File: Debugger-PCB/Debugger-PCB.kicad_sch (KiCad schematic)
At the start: 0 parts

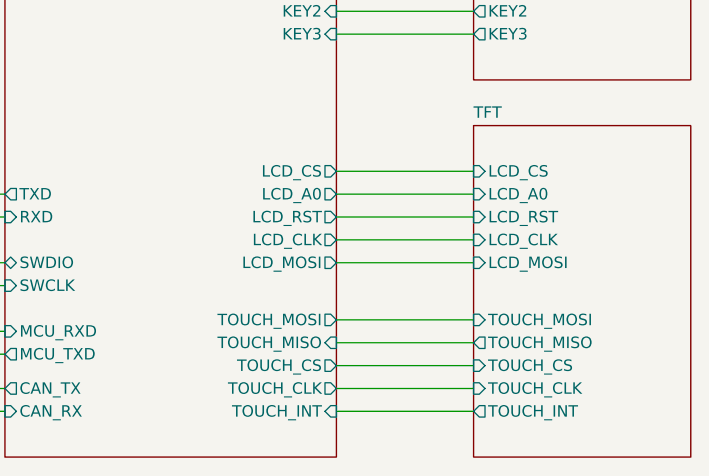
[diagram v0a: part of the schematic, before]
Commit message: fix some details of PCB
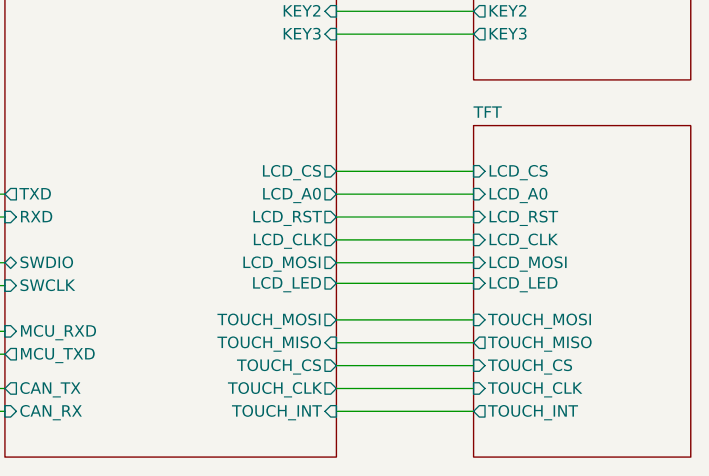
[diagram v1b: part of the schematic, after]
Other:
- sheet MCU ports: added LCD_LED; removed none
- sheet TFT ports: added LCD_LED; removed none
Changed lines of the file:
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@@
+    (stroke (width 0) (type default) (color 0 0 0 0))
+  )
+  (wire (pts (xy 222.25 159.766) (xy 237.49 159.766))
     (stroke (width 0) (type default) (color 0 0 0 0))
   )
@@
       (effects (font (size 1.27 1.27)) (justify left))
     )
+    (pin "LCD_LED" input (at 237.49 159.766 180)
+      (effects (font (size 1.27 1.27)) (justify left))
+    )
   )
   (sheet (at 185.42 114.3) (size 36.83 64.77) (fields_autoplaced)
@@
     )
     (pin "KEY3" input (at 222.25 132.08 0)
+      (effects (font (size 1.27 1.27)) (justify right))
+    )
+    (pin "LCD_LED" output (at 222.25 159.766 0)
       (effects (font (size 1.27 1.27)) (justify right))
     )
@@
       (reference "#PWR057") (unit 1) (value "VCC") (footprint "")
     )
-    (path "/98507381-f2ba-4111-8a0c-685d3bb1dc73/edf7fd00-56a4-4615-95df-5a269d3d723f"
-      (reference "#PWR058") (unit 1) (value "VCC") (footprint "")
-    )
     (path "/98507381-f2ba-4111-8a0c-685d3bb1dc73/6f52f786-b4c0-44b2-8071-17e39d084c29"
       (reference "#PWR059") (unit 1) (value "GND") (footprint "")
@@
       (reference "#PWR062") (unit 1) (value "GND") (footprint "")
     )
-    (path "/98507381-f2ba-4111-8a0c-685d3bb1dc73/292a4533-a85c-478c-bb48-f8e44071f858"
-      (reference "#PWR063") (unit 1) (value "GND") (footprint "")
-    )
-    (path "/98507381-f2ba-4111-8a0c-685d3bb1dc73/25948667-45ee-4c9f-9351-e19cee2c4d2a"
-      (reference "#PWR064") (unit 1) (value "GND") (footprint "")
-    )
     (path "/f62c1f79-9897-417c-80b5-375c0b215cca/4a0eda2d-a0f5-4497-b46a-c4cec8ad4931"
       (reference "#PWR0101") (unit 1) (value "VCC") (footprint "")
@@
       (reference "#PWR0103") (unit 1) (value "VCC") (footprint "")
     )
+    (path "/42df1dfa-ab2e-460c-8753-1de9db40f85a/baab9947-9bf5-42ec-8dc5-e6ae9b5f2e9b"
+      (reference "#PWR0104") (unit 1) (value "GND") (footprint "")
+    )
+    (path "/42df1dfa-ab2e-460c-8753-1de9db40f85a/f939aabb-c7c0-47c1-b5fa-85c2748b9d86"
+      (reference "#PWR0105") (unit 1) (value "GND") (footprint "")
+    )
+    (path "/b0467b07-32de-468c-a83e-6fe96781bcfe/2d9aa523-584c-4e58-ae94-1b029770dc75"
+      (reference "#PWR0106") (unit 1) (value "GND") (footprint "")
+    )
     (path "/42df1dfa-ab2e-460c-8753-1de9db40f85a/540b8823-2d1b-4a52-81d3-ade6ac974afd"
       (reference "C1") (unit 1) (value "10u") (footprint "Capacitor_SMD:C_0603_1608Metric")
@@
       (reference "C27") (unit 1) (value "100n") (footprint "Capacitor_SMD:C_0603_1608Metric")
     )
-    (path "/98507381-f2ba-4111-8a0c-685d3bb1dc73/6a646482-4975-41ee-9572-2521e9033ad1"
-      (reference "C28") (unit 1) (value "100n") (footprint "Capacitor_SMD:C_0603_1608Metric")
-    )
     (path "/42df1dfa-ab2e-460c-8753-1de9db40f85a/5e8b8d06-e040-4890-a404-eecea5d84e0f"
       (reference "D1") (unit 1) (value "LED") (footprint "LED_SMD:LED_0603_1608Metric")
@@
       (reference "LCD1") (unit 1) (value "1.8inch-TFT-LCD") (footprint "debugger:TFT-LCD1.8inch")
     )
+    (path "/b0467b07-32de-468c-a83e-6fe96781bcfe/99520a95-636f-4c5f-8c4f-c2d2aa10850a"
+      (reference "Q1") (unit 1) (value "S8050") (footprint "Package_TO_SOT_SMD:SOT-23")
+    )
     (path "/42df1dfa-ab2e-460c-8753-1de9db40f85a/31351644-d0ab-4db7-bb3f-ffb9945168e5"
       (reference "R1") (unit 1) (value "1k") (footprint "Resistor_SMD:R_0603_1608Metric")
@@
       (reference "R8") (unit 1) (value "1k") (footprint "Resistor_SMD:R_0603_1608Metric")
     )
-    (path "/98507381-f2ba-4111-8a0c-685d3bb1dc73/16799d5f-acaa-43dd-810c-812bd0dd975f"
-      (reference "R9") (unit 1) (value "1k") (footprint "Resistor_SMD:R_0603_1608Metric")
+    (path "/42df1dfa-ab2e-460c-8753-1de9db40f85a/dcd64286-eb78-45d3-acb5-462a22521c32"
+      (reference "R10") (unit 1) (value "10k") (footprint "Resistor_SMD:R_0603_1608Metric")
+    )
+    (path "/42df1dfa-ab2e-460c-8753-1de9db40f85a/7a0d6825-3f2c-45a4-9b96-0229f9750a3d"
+      (reference "R11") (unit 1) (value "10k") (footprint "Resistor_SMD:R_0603_1608Metric")
+    )
+    (path "/b0467b07-32de-468c-a83e-6fe96781bcfe/59b81b29-0388-4a91-9e62-7582c5face23"
+      (reference "R12") (unit 1) (value "R") (footprint "GENERAL_RCL_SMD:L0603(1608M)")
     )
     (path "/98507381-f2ba-4111-8a0c-685d3bb1dc73/23aa22bb-7f65-4192-a5a4-07ac1a9976d3"
-      (reference "SW3") (unit 1) (value "SW_Push") (footprint "MyLib:SW_YD-3410")
+      (reference "SW3") (unit 1) (value "SW_Push") (footprint "debugger:button")
     )
     (path "/98507381-f2ba-4111-8a0c-685d3bb1dc73/396cacc5-f3d0-4c1c-95a1-3318593d5ae9"
-      (reference "SW4") (unit 1) (value "SW_Push") (footprint "MyLib:SW_YD-3410")
-    )
-    (path "/98507381-f2ba-4111-8a0c-685d3bb1dc73/91387858-b6a0-437a-a24a-73cbeeacf1d6"
-      (reference "SW5") (unit 1) (value "SW_Push") (footprint "MyLib:SW_YD-3410")
+      (reference "SW4") (unit 1) (value "SW_Push") (footprint "debugger:button")
     )
     (path "/42df1dfa-ab2e-460c-8753-1de9db40f85a/f4182f70-5fe6-4caa-93b9-9ff7dd052083"

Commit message: temp.change the PCB.And change the code.
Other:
- removed sheet TFT
- sheet MCU ports: added ADC1_IN0, ADC1_IN1, ADC1_IN11, ADC1_IN12, ADC1_IN13, ADC1_IN14, I2C3_SCL, I2C3_SDA, KEY4, KEY5, LCD_CS0, LCD_DC, RESET, TIM1_CH1, TIM1_CH2, TIM3_CH1, TIM3_CH2, TIM4_CH1, TIM4_CH2; removed none
- sheet Power&Port ports: added ADC1_IN0, ADC1_IN1, ADC1_IN11, ADC1_IN12, ADC1_IN13, ADC1_IN14, I2C3_SCL, I2C3_SDA, KEY1, KEY2, KEY3, KEY4, KEY5, LCD_A0, LCD_CLK, LCD_CS, LCD_CS0, LCD_DC, LCD_LED, LCD_MOSI, LCD_RST, RESET, TIM1_CH1, TIM1_CH2, TIM3_CH1, TIM3_CH2, TIM4_CH1, TIM4_CH2, TOUCH_CLK, TOUCH_CS, TOUCH_INT, TOUCH_MISO, TOUCH_MOSI, VCC; removed none
